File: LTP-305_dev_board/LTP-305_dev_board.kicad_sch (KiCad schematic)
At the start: 27 parts, among them J1 Conn_01x14, J10 Conn_01x04, J11 Conn_01x04, J12 Conn_01x04, J13 Conn_01x04, J14 Conn_01x04, J15 Conn_01x04, J2 Conn_01x14, J3 Conn_01x14, J4 Conn_01x14, J5 Conn_01x07, J6 Conn_01x07, J7 Conn_01x04, J8 Conn_01x04, J9 Conn_01x04, U1 IS31FL3731-SA

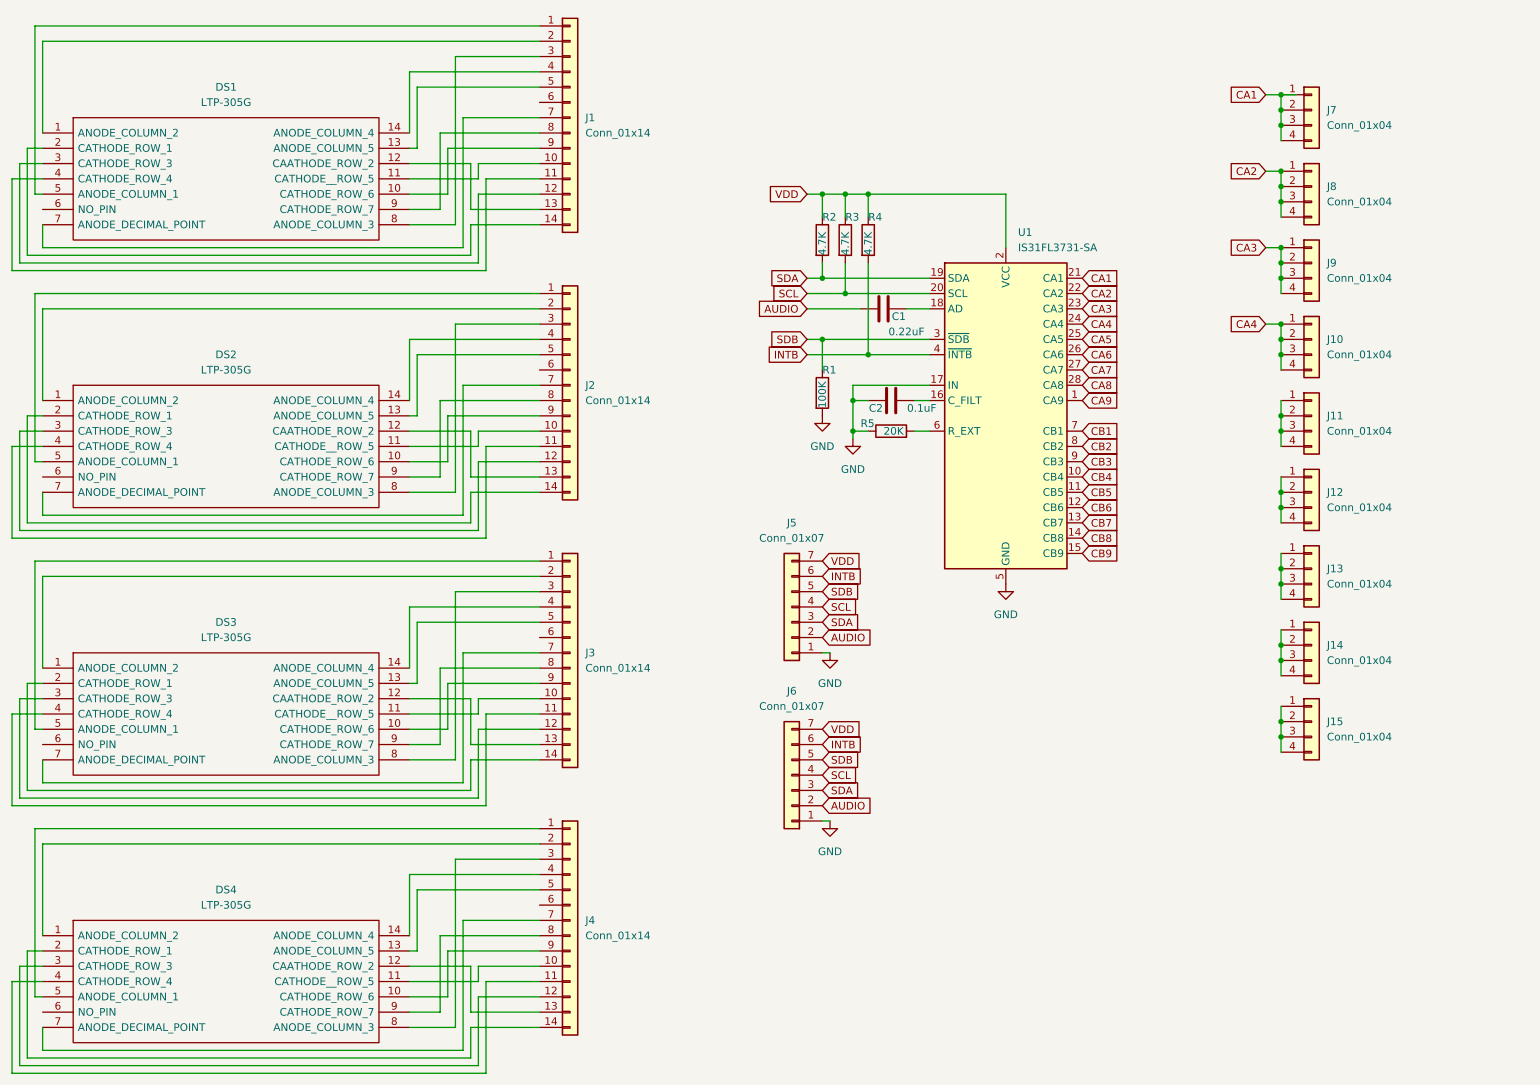
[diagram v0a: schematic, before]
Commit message: Changes in schematics and PCB layout
Added power control LED
Finished schematics
New PCB layout
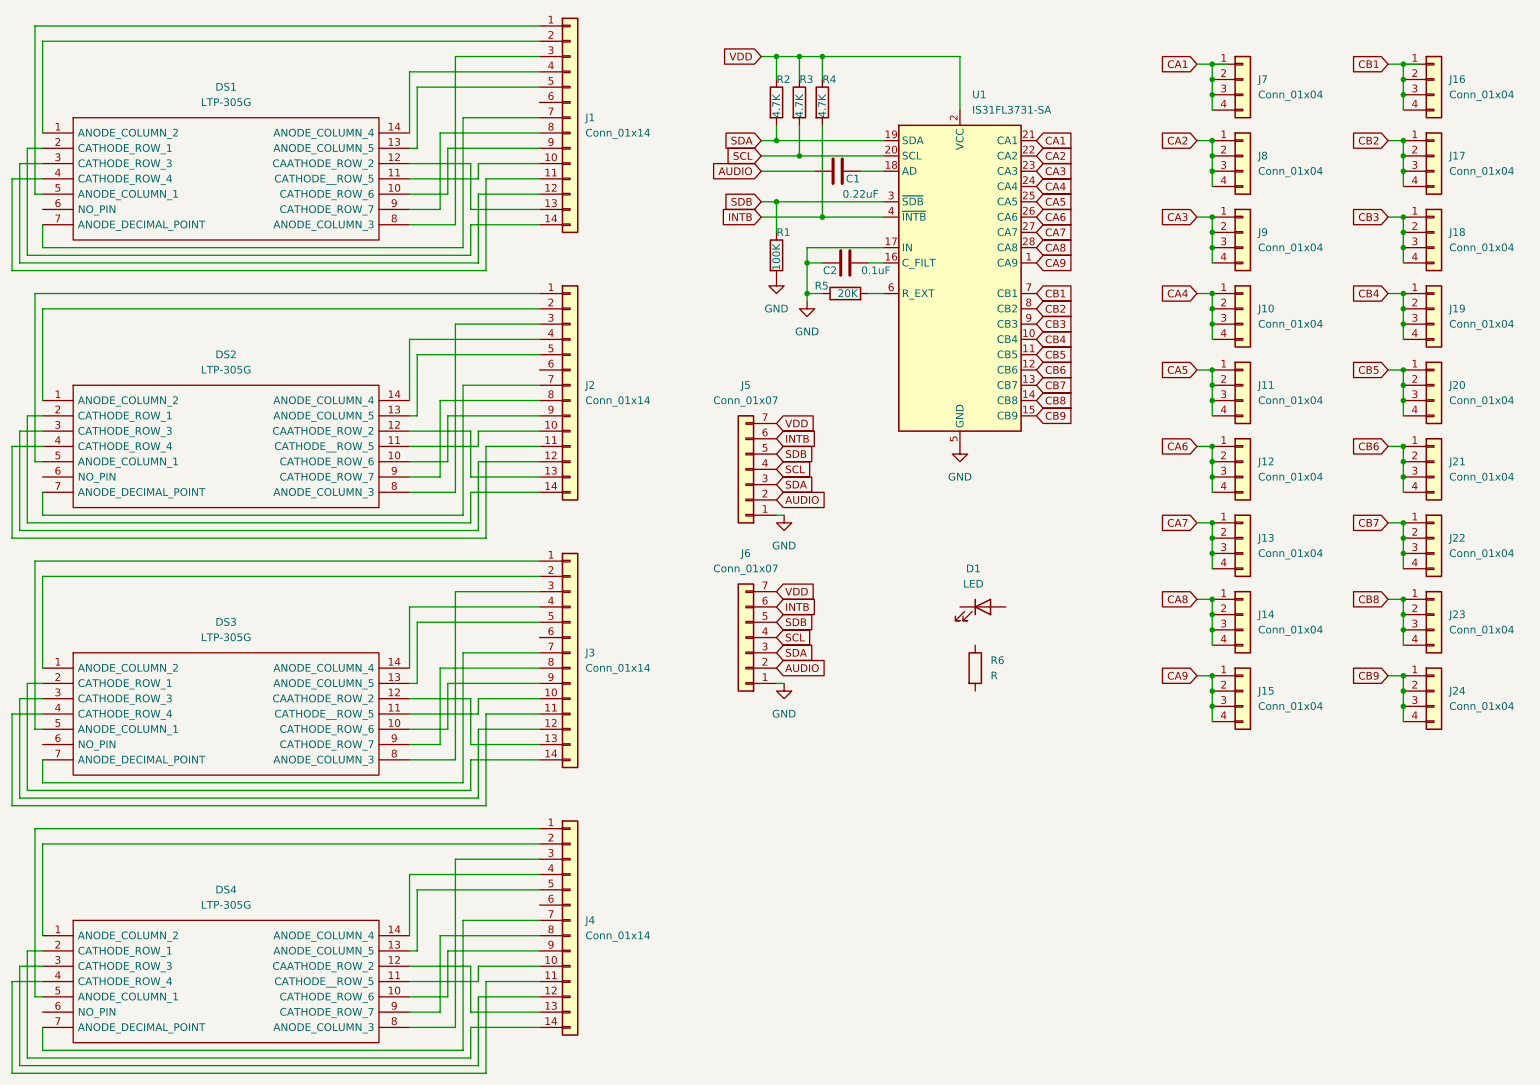
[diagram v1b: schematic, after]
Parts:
- added D1: LED, symbol Device:LED
- added J16, J17, J18, J19, J20, J21, J22, J23, J24: Conn_01x04, Connector_PinHeader_1.27mm:PinHeader_1x04_P1.27mm_Vertical, symbol Connector_Generic:Conn_01x04
- added R6: R, symbol Device:R
- J10, J11, J12, J13, J14, J15, J8, J9: footprint Connector_PinSocket_1.27mm:PinSocket_1x04_P1.27mm_Vertical -> Connector_PinHeader_1.27mm:PinHeader_1x04_P1.27mm_Vertical
- J5: footprint Connector_PinSocket_2.54mm:PinSocket_1x07_P2.54mm_Vertical -> Connector_PinHeader_2.54mm:PinHeader_1x07_P2.54mm_Vertical
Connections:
- net CA5: now also J11.1 (Pin_1), J11.2 (Pin_2), J11.3 (Pin_3), J11.4 (Pin_4)
- net CA6: now also J12.1 (Pin_1), J12.2 (Pin_2), J12.3 (Pin_3), J12.4 (Pin_4)
- net CA7: now also J13.1 (Pin_1), J13.2 (Pin_2), J13.3 (Pin_3), J13.4 (Pin_4)
- net CA8: now also J14.1 (Pin_1), J14.2 (Pin_2), J14.3 (Pin_3), J14.4 (Pin_4)
- net CA9: now also J15.1 (Pin_1), J15.2 (Pin_2), J15.3 (Pin_3), J15.4 (Pin_4)
- net CB1: now also J16.1 (Pin_1), J16.2 (Pin_2), J16.3 (Pin_3), J16.4 (Pin_4)
- net CB2: now also J17.1 (Pin_1), J17.2 (Pin_2), J17.3 (Pin_3), J17.4 (Pin_4)
- net CB3: now also J18.1 (Pin_1), J18.2 (Pin_2), J18.3 (Pin_3), J18.4 (Pin_4)
- net CB4: now also J19.1 (Pin_1), J19.2 (Pin_2), J19.3 (Pin_3), J19.4 (Pin_4)
- net CB5: now also J20.1 (Pin_1), J20.2 (Pin_2), J20.3 (Pin_3), J20.4 (Pin_4)
- net CB6: now also J21.1 (Pin_1), J21.2 (Pin_2), J21.3 (Pin_3), J21.4 (Pin_4)
- net CB7: now also J22.1 (Pin_1), J22.2 (Pin_2), J22.3 (Pin_3), J22.4 (Pin_4)
- net CB8: now also J23.1 (Pin_1), J23.2 (Pin_2), J23.3 (Pin_3), J23.4 (Pin_4)
- net CB9: now also J24.1 (Pin_1), J24.2 (Pin_2), J24.3 (Pin_3), J24.4 (Pin_4)
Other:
- moved on the sheet: C1, C2, J10, J11, J12, J13, J14, J15, J5, J6, J7, J8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

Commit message: Board layout update
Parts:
- D1: footprint (none) -> LED_SMD:LED_0603_1608Metric_Pad1.05x0.95mm_HandSolder
- R6: footprint (none) -> Resistor_SMD:R_0603_1608Metric_Pad0.98x0.95mm_HandSolder
- renumbered J7 to CA1, J8 to CA2, J9 to CA3, J10 to CA4, J11 to CA5, J12 to CA6, J13 to CA7, J14 to CA8, J15 to CA9, J16 to CB1, J17 to CB2, J18 to CB3, J19 to CB4, J20 to CB5, J21 to CB6, J22 to CB7, J23 to CB8, J24 to CB9
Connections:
- net GND: now also D1.2 (A)
- net VDD: now also R6.1
- net at R6.2: now also D1.1 (K)
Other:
- moved on the sheet: R6

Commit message: rev 0.1 done
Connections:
- net GND: now also D1.1 (K); no longer D1.2 (A)
- net at R6.2: now also D1.2 (A); no longer D1.1 (K)
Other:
- moved on the sheet: D1
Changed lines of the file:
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@@
     (pin "9")
   )
-  (symbol (lib_id "Device:LED") (at 182.88 114.3 0) (unit 1)
+  (symbol (lib_id "Device:LED") (at 182.88 114.3 180) (unit 1)
     (in_bom yes) (on_board yes) (fields_autoplaced)
-    (property "Reference" "D1" (id 0) (at 181.2925 107.95 0))
-    (property "Value" "LED" (id 1) (at 181.2925 110.49 0))
+    (property "Reference" "D1" (id 0) (at 184.4675 106.68 0))
+    (property "Value" "LED" (id 1) (at 184.4675 109.22 0))
     (property "Footprint" "LED_SMD:LED_0603_1608Metric_Pad1.05x0.95mm_HandSolder" (id 2) (at 182.88 114.3 0)
       (effects (font (size 1.27 1.27)) hide)

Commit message: Minor changes
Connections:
- no-connect marks 0 -> 8
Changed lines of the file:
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@@
   (junction (at 252.73 67.31) (diameter 0) (color 0 0 0 0)
   )
+  (no_connect (at 26.67 92.71))
+  (no_connect (at 109.22 74.93))
+  (no_connect (at 109.22 119.38))
+  (no_connect (at 26.67 137.16))
+  (no_connect (at 109.22 163.83))
+  (no_connect (at 26.67 181.61))
+  (no_connect (at 26.67 48.26))
+  (no_connect (at 109.22 30.48))
   (wire (pts (xy 88.9 72.39) (xy 109.22 72.39))
     (stroke (width 0) (type default) (color 0 0 0 0))
@@
     (pin "9")
   )
+  (symbol (lib_id "power:PWR_FLAG") (at 152.4 22.86 0) (unit 1)
+    (in_bom yes) (on_board yes) (fields_autoplaced)
+    (property "Reference" "#FLG0101" (id 0) (at 152.4 20.955 0)
+      (effects (font (size 1.27 1.27)) hide)
+    )
+    (property "Value" "PWR_FLAG" (id 1) (at 152.4 17.78 0))
+    (property "Footprint" "" (id 2) (at 152.4 22.86 0)
+      (effects (font (size 1.27 1.27)) hide)
+    )
+    (property "Datasheet" "~" (id 3) (at 152.4 22.86 0)
+      (effects (font (size 1.27 1.27)) hide)
+    )
+    (pin "1")
+  )
   (symbol (lib_id "Connector_Generic:Conn_01x04") (at 226.06 64.77 0) (unit 1)
     (in_bom yes) (on_board yes) (fields_autoplaced)
@@
   )
   (symbol_instances
+    (path "/4145fb02-c33b-445a-8eb8-0d2ac30ffa11"
+      (reference "#FLG0101") (unit 1) (value "PWR_FLAG") (footprint "")
+    )
     (path "/f1eac795-a34a-452d-b860-d91e81ec0549"
       (reference "#PWR0101") (unit 1) (value "GND") (footprint "")

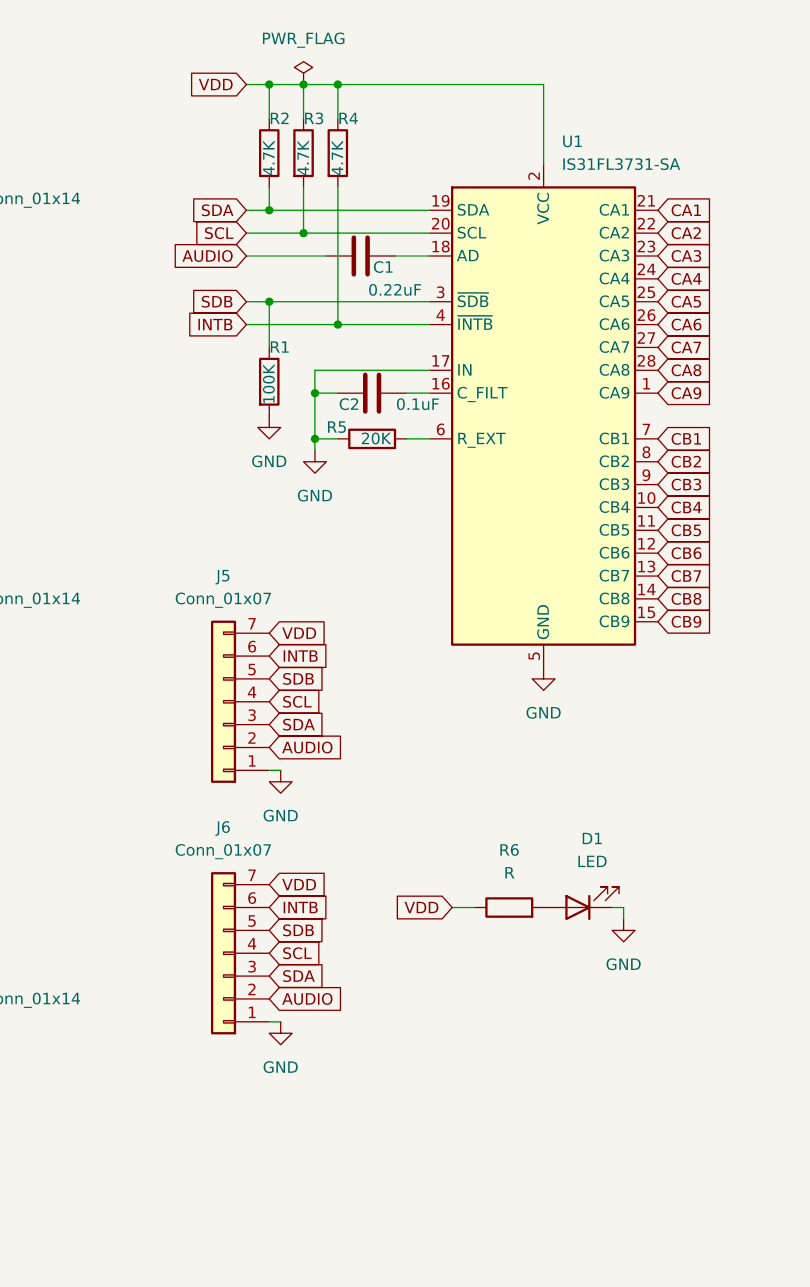
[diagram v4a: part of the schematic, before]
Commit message: Changes in board layout
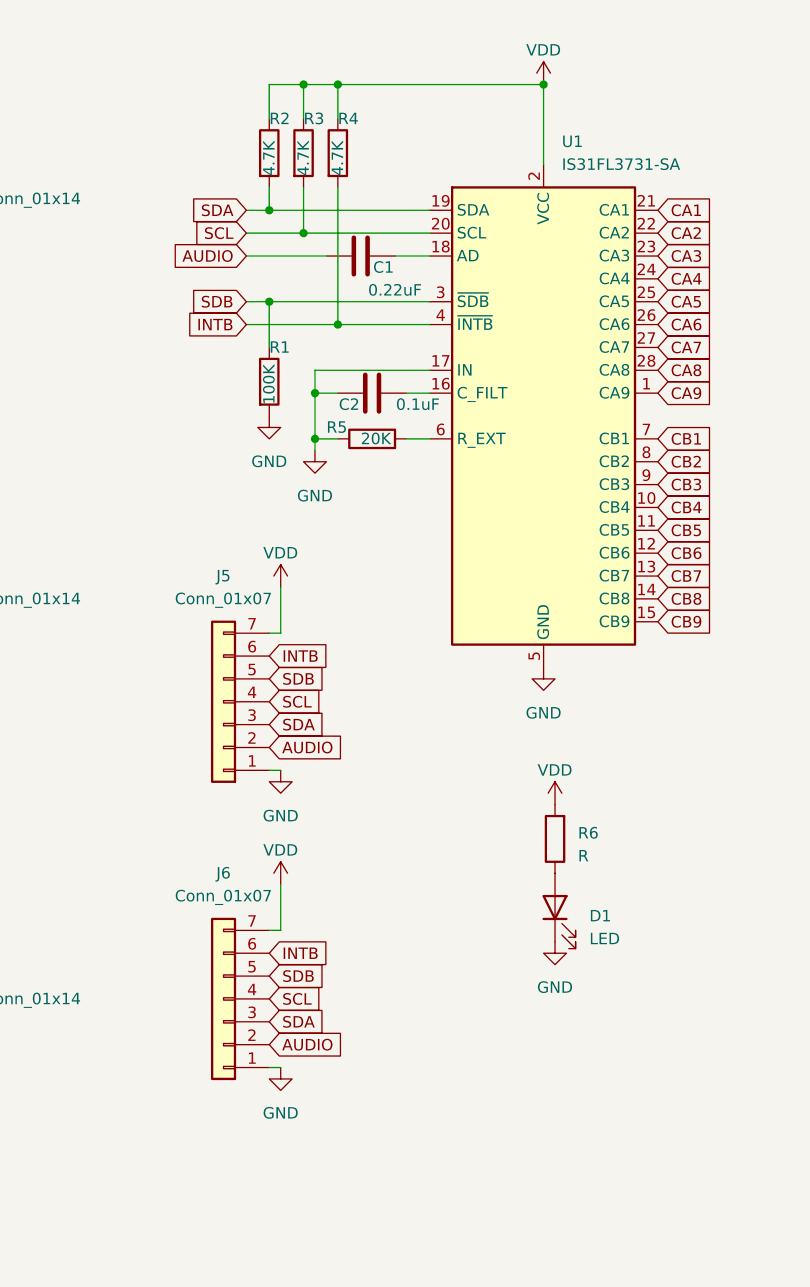
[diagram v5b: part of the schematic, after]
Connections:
- net VDD: now also R6.2; no longer R6.1
- net at D1.2 (A): now also R6.1; no longer R6.2
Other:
- moved on the sheet: D1, J6, R6
